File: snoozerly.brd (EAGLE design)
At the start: 70 x 43 mm, 57 parts, among them Q2 MOSFET-NCHANNELFDD8780, Q3 MOSFET-NCHANNELBSS123LT1G, Q4 MOSFET-NCHANNELBSS123LT1G, U1 ATMEGA328P, Y1 32KHz, Y2 8MHz

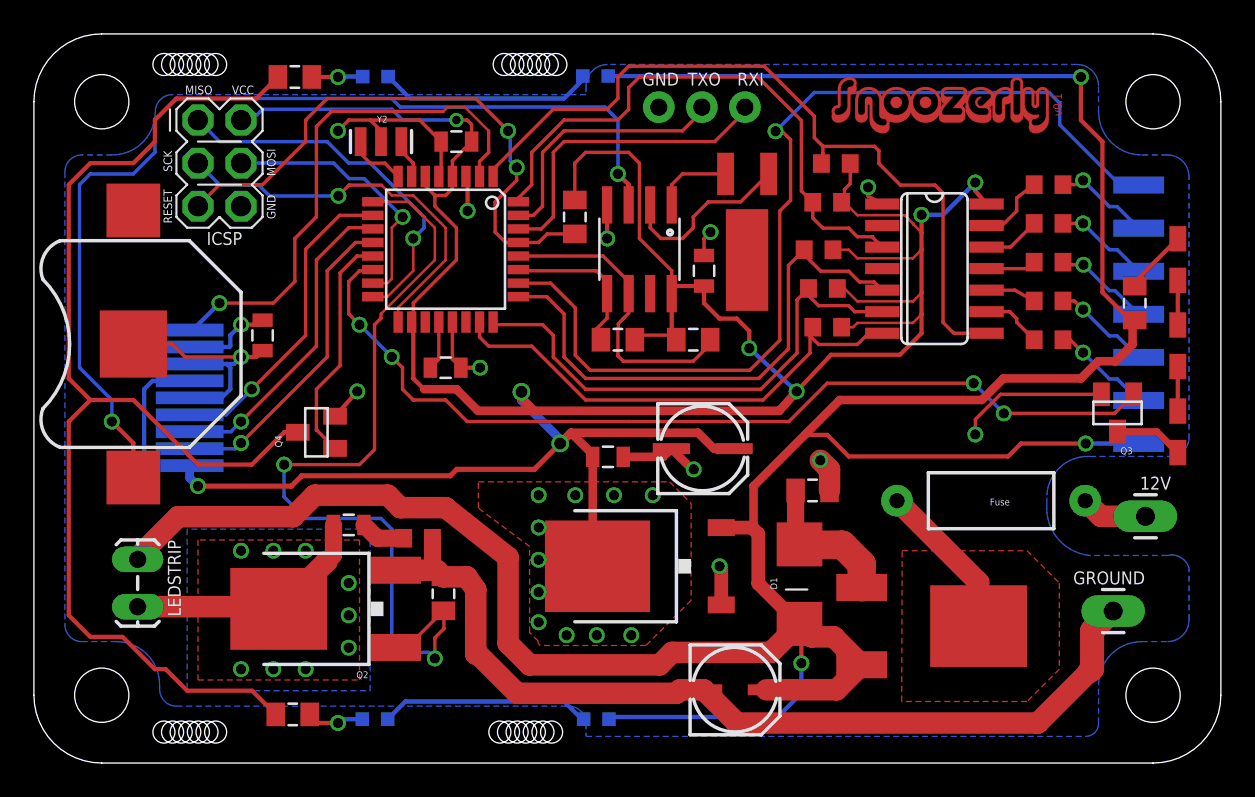
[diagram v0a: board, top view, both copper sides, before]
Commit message: update pchannel footprint and fixed spacings
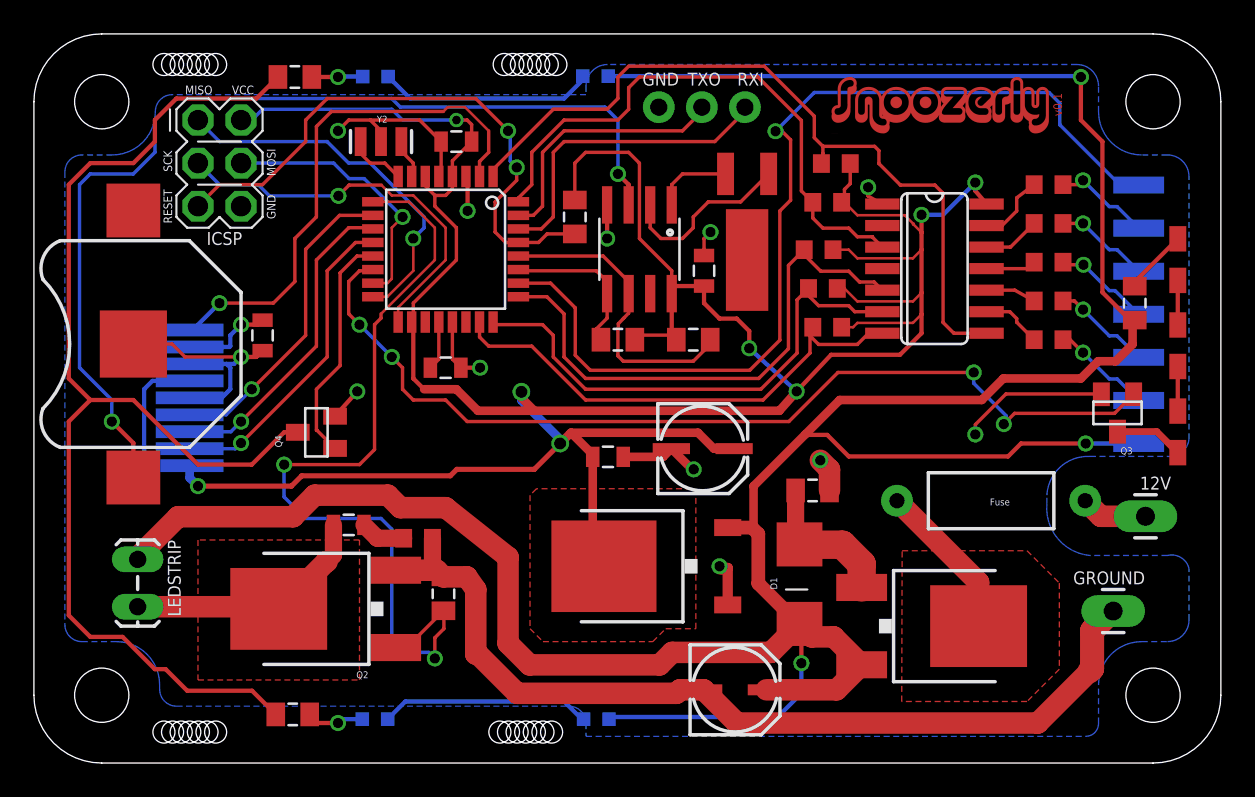
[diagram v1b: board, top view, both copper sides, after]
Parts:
- removed U$26: VREG-3.3VNCP1117, jt_parts:TO-252
- added NCP1117: VREG-3.3VNCP1117, jt_parts:TO-252
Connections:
- net 12V: now also NCP1117.3; no longer U$26.3
- net 5V: now also NCP1117.2; no longer U$26.2
- net GND: now also NCP1117.1; no longer U$26.1
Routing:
- net NIGHT_LIGHT: track 55.4 -> 57.3 mm
- net N$14: vias 9 -> 0
- removed copper zone on layer 16, net N$14
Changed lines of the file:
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@@
 <attribute name="VALUE" x="23.876" y="14.859" size="0.4064" layer="27" rot="R180"/>
 </element>
-<element name="U$26" library="jt_parts" package="TO-252" value="VREG-3.3VNCP1117" x="34.925" y="12.065" rot="R90"/>
+<element name="NCP1117" library="jt_parts" package="TO-252" value="VREG-3.3VNCP1117" x="35.306" y="12.065" rot="R90"/>
 </elements>
 <signals>
@@
 <contactref element="GROUND" pad="1"/>
 <wire x1="62.7126" y1="5.8674" x2="59.6646" y2="2.8194" width="1.27" layer="1"/>
-<wire x1="63.4136" y1="22.2074" x2="57.4626" y2="22.2074" width="0.2032" layer="1"/>
-<wire x1="57.4626" y1="22.2074" x2="55.9816" y2="20.7264" width="0.2032" layer="1"/>
 <via x="55.9816" y="19.8374" extent="1-16" drill="0.6"/>
-<wire x1="55.9816" y1="20.7264" x2="55.9816" y2="19.8374" width="0.2032" layer="1"/>
 <via x="26.035" y="33.02" extent="1-16" drill="0.6"/>
 <wire x1="26.035" y1="33.02" x2="26.035" y2="34.9566" width="0.254" layer="1"/>
@@
 <wire x1="47.3804" y1="17.7706" x2="46.8376" y2="18.3134" width="1.27" layer="1"/>
 <contactref element="SERIAL" pad="1"/>
-<contactref element="U$26" pad="1"/>
+<contactref element="NCP1117" pad="1"/>
 <via x="40.894" y="12.065" extent="1-16" drill="0.6"/>
-<wire x1="40.995" y1="9.785" x2="40.995" y2="11.964" width="0.8128" layer="1"/>
 <wire x1="40.995" y1="11.964" x2="40.894" y2="12.065" width="0.8128" layer="1"/>
 <wire x1="35.2154" y1="18.5166" x2="37.5668" y2="18.5166" width="0.508" layer="1"/>
 <wire x1="37.5668" y1="18.5166" x2="38.0526" y2="19.0024" width="0.508" layer="1"/>
 <via x="39.37" y="17.78" extent="1-16" drill="0.6"/>
-<wire x1="64.1096" y1="9.4996" x2="64.1096" y2="9.4234" width="0" layer="19" extent="1-1"/>
 <wire x1="39.37" y1="17.78" x2="39.275" y2="17.78" width="0.508" layer="1"/>
 <wire x1="39.275" y1="17.78" x2="38.0526" y2="19.0024" width="0.508" layer="1"/>
+<wire x1="40.995" y1="11.964" x2="41.376" y2="11.964" width="0.6096" layer="1"/>
+<wire x1="41.376" y1="11.964" x2="41.376" y2="9.785" width="0.6096" layer="1"/>
+<wire x1="55.9816" y1="19.8374" x2="55.9816" y2="20.4216" width="0.2032" layer="1"/>
+<wire x1="55.9816" y1="20.4216" x2="57.785" y2="22.225" width="0.2032" layer="1"/>
+<wire x1="57.785" y1="22.225" x2="63.396" y2="22.225" width="0.2032" layer="1"/>
+<wire x1="63.396" y1="22.225" x2="63.4136" y2="22.2074" width="0.2032" layer="1"/>
+<wire x1="64.1096" y1="9.4234" x2="64.1096" y2="9.4996" width="0" layer="19" extent="1-1"/>
 </signal>
 <signal name="5V" class="2">
@@
 <wire x1="25.4" y1="17.78" x2="29.972" y2="17.78" width="0.3048" layer="1"/>
 <wire x1="29.972" y1="17.78" x2="31.496" y2="19.304" width="0.3048" layer="1"/>
-<contactref element="U$26" pad="2"/>
-<polygon width="0" layer="1" thermals="no">
-<vertex x="29.6926" y="8.1534"/>
-<vertex x="29.6926" y="13.2334"/>
-<vertex x="26.67" y="15.494"/>
-<vertex x="26.67" y="17.0434"/>
-<vertex x="37.9476" y="17.0434"/>
-<vertex x="39.2176" y="15.7734"/>
-<vertex x="39.2176" y="10.0584"/>
-<vertex x="36.5506" y="7.3914"/>
-<vertex x="30.3276" y="7.3914"/>
-<vertex x="30.2006" y="7.5184"/>
-<vertex x="30.2006" y="7.6454"/>
-</polygon>
+<contactref element="NCP1117" pad="2"/>
 <wire x1="41.3226" y1="19.0024" x2="40.5606" y2="19.0024" width="0.508" layer="1"/>
 <wire x1="40.5606" y1="19.0024" x2="39.624" y2="19.939" width="0.508" layer="1"/>
@@
 <wire x1="33.4154" y1="18.6546" x2="32.131" y2="19.939" width="0.508" layer="1"/>
 <wire x1="33.4154" y1="18.5166" x2="33.4154" y2="12.3446" width="0.508" layer="1"/>
-<wire x1="33.4154" y1="12.3446" x2="33.695" y2="12.065" width="0.508" layer="1"/>
+<wire x1="33.4154" y1="12.3446" x2="34.076" y2="12.065" width="0.508" layer="1"/>
+<polygon width="0.0254" layer="1" thermals="no">
+<vertex x="29.718" y="16.256"/>
+<vertex x="29.718" y="8.382"/>
+<vertex x="30.48" y="7.62"/>
+<vertex x="36.957" y="7.62"/>
+<vertex x="37.719" y="8.382"/>
+<vertex x="39.497" y="8.382"/>
+<vertex x="39.497" y="16.383"/>
+<vertex x="39.243" y="16.637"/>
+<vertex x="30.099" y="16.637"/>
+</polygon>
 </signal>
 <signal name="N$64">
@@
 <wire x1="17.018" y1="16.256" x2="15.748" y2="14.986" width="1.27" layer="1"/>
 <wire x1="15.748" y1="14.986" x2="8.9662" y2="14.986" width="1.27" layer="1"/>
-<contactref element="U$26" pad="3"/>
+<contactref element="NCP1117" pad="3"/>
 <wire x1="37.3634" y1="6.2484" x2="38.1" y2="6.985" width="1.27" layer="1"/>
 <wire x1="38.1" y1="6.985" x2="43.9322" y2="6.985" width="1.27" layer="1"/>
 <wire x1="43.9322" y1="6.985" x2="45.6106" y2="8.6634" width="1.27" layer="1"/>
-<wire x1="40.995" y1="14.345" x2="42.805" y2="14.345" width="0.8128" layer="1"/>
+<wire x1="41.376" y1="14.345" x2="42.805" y2="14.345" width="0.8128" layer="1"/>
 <wire x1="42.805" y1="14.345" x2="43.18" y2="13.97" width="0.8128" layer="1"/>
 <wire x1="43.18" y1="13.97" x2="43.18" y2="11.049" width="0.8128" layer="1"/>
@@
 <vertex x="19.6596" y="5.3594"/>
 </polygon>
-<via x="16.4846" y="5.9944" extent="1-16" drill="0.6"/>
-<via x="14.5796" y="5.9944" extent="1-16" drill="0.6"/>
-<via x="12.6746" y="5.9944" extent="1-16" drill="0.6"/>
-<via x="16.4846" y="12.9794" extent="1-16" drill="0.6"/>
-<via x="14.5796" y="12.9794" extent="1-16" drill="0.6"/>
-<via x="12.6746" y="12.9794" extent="1-16" drill="0.6"/>
-<via x="19.0246" y="7.2644" extent="1-16" drill="0.6"/>
-<via x="19.0246" y="11.0744" extent="1-16" drill="0.6"/>
-<polygon width="0" layer="16" thermals="no">
-<vertex x="20.2946" y="4.7244"/>
-<vertex x="20.2946" y="14.2494"/>
-<vertex x="9.4996" y="14.2494"/>
-<vertex x="9.4996" y="4.7244"/>
-</polygon>
 <wire x1="17.7546" y1="12.3444" x2="17.7146" y2="12.3444" width="1.27" layer="1"/>
 <wire x1="17.7146" y1="12.3444" x2="15.2146" y2="9.8444" width="1.27" layer="1"/>
@@
 <wire x1="15.2146" y1="9.8044" x2="15.1506" y2="9.8044" width="1.27" layer="1"/>
 <wire x1="15.1506" y1="9.8044" x2="14.8966" y2="9.5504" width="1.27" layer="1"/>
-<via x="19.0246" y="9.1694" extent="1-16" drill="0.6"/>
 <wire x1="6.5786" y1="9.6774" x2="15.7226" y2="9.6774" width="1.27" layer="1"/>
 <wire x1="15.7226" y1="9.6774" x2="16.51" y2="8.89" width="1.27" layer="1"/>
@@
 <wire x1="26.0096" y1="20.5994" x2="24.7396" y2="21.8694" width="0.2032" layer="1"/>
 <wire x1="24.7396" y1="21.8694" x2="22.8346" y2="21.8694" width="0.2032" layer="1"/>
-<wire x1="35.5346" y1="20.5994" x2="26.0096" y2="20.5994" width="0.2032" layer="1"/>
+<wire x1="44.9834" y1="20.5994" x2="26.0096" y2="20.5994" width="0.2032" layer="1"/>
 <wire x1="22.8346" y1="21.8694" x2="22.1996" y2="22.5044" width="0.2032" layer="1"/>
 <wire x1="22.1996" y1="22.5044" x2="22.1996" y2="23.7744" width="0.2032" layer="1"/>
@@
 <wire x1="19.6596" y1="29.4894" x2="20.377" y2="29.4894" width="0.2032" layer="1"/>
 <wire x1="20.377" y1="29.4894" x2="20.447" y2="29.5594" width="0.2032" layer="1"/>
-<wire x1="35.5346" y1="20.5994" x2="44.9834" y2="20.5994" width="0.2032" layer="1"/>
-<wire x1="44.9834" y1="20.5994" x2="47.244" y2="22.86" width="0.2032" layer="1"/>
-<wire x1="47.244" y1="22.86" x2="55.88" y2="22.86" width="0.2032" layer="1"/>
-<via x="55.88" y="22.86" extent="1-16" drill="0.6"/>
-<via x="57.658" y="21.082" extent="1-16" drill="0.6"/>
-<wire x1="57.658" y1="21.082" x2="64.1882" y2="21.082" width="0.2032" layer="1"/>
+<wire x1="44.9834" y1="20.5994" x2="47.879" y2="23.495" width="0.2032" layer="1"/>
+<via x="55.88" y="23.495" extent="1-16" drill="0.6"/>
+<via x="57.658" y="20.447" extent="1-16" drill="0.6"/>
 <wire x1="64.1882" y1="21.082" x2="65.3136" y2="22.2074" width="0.2032" layer="1"/>
-<wire x1="57.658" y1="21.082" x2="55.88" y2="22.86" width="0.2032" layer="16"/>
+<wire x1="55.88" y1="23.495" x2="47.879" y2="23.495" width="0.2032" layer="1"/>
+<wire x1="64.1882" y1="21.082" x2="58.293" y2="21.082" width="0.2032" layer="1"/>
+<wire x1="58.293" y1="21.082" x2="57.658" y2="20.447" width="0.2032" layer="1"/>
+<wire x1="55.88" y1="23.495" x2="55.88" y2="22.86" width="0.2032" layer="16"/>
+<wire x1="55.88" y1="22.86" x2="57.785" y2="20.955" width="0.2032" layer="16"/>
+<wire x1="57.785" y1="20.955" x2="57.785" y2="20.574" width="0.2032" layer="16"/>
+<wire x1="57.785" y1="20.574" x2="57.658" y2="20.447" width="0.2032" layer="16"/>
 </signal>
 <signal name="N$19">
@@
 <wire x1="20.712" y1="13.716" x2="19.9246" y2="14.5034" width="1.016" layer="1"/>
 </signal>
-<signal name="N$24">
-<via x="34.671" y="16.256" extent="1-16" drill="0.6"/>
-</signal>
-<signal name="N$25">
-<via x="32.385" y="16.256" extent="1-16" drill="0.6"/>
-</signal>
-<signal name="N$26">
-<via x="36.957" y="16.256" extent="1-16" drill="0.6"/>
-</signal>
-<signal name="N$27">
-<via x="30.226" y="16.256" extent="1-16" drill="0.6"/>
-</signal>
-<signal name="N$29">
-<via x="30.226" y="14.351" extent="1-16" drill="0.6"/>
-</signal>
-<signal name="N$34">
-<via x="30.226" y="12.446" extent="1-16" drill="0.6"/>
-</signal>
-<signal name="N$35">
-<via x="30.226" y="10.541" extent="1-16" drill="0.6"/>
-</signal>
-<signal name="N$36">
-<via x="30.226" y="8.763" extent="1-16" drill="0.6"/>
-</signal>
-<signal name="N$37">
-<via x="31.877" y="8.001" extent="1-16" drill="0.6"/>
-</signal>
-<signal name="N$38">
-<via x="33.655" y="8.001" extent="1-16" drill="0.6"/>
-</signal>
-<signal name="N$39">
-<via x="35.687" y="8.001" extent="1-16" drill="0.6"/>
-</signal>
 </signals>

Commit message: Merge branch 'master' into rev-0.1
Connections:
- net PWM_LED renamed PWM_STRIP
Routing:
- net PWM_STRIP: track 49.9 -> 47.8 mm
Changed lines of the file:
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@@
 <wire x1="24.8666" y1="39.1414" x2="25.8826" y2="39.1414" width="0.1524" layer="1"/>
-</signal>
-<signal name="PWM_LED">
-<contactref element="U1" pad="9"/>
-<contactref element="U$15" pad="2"/>
-<contactref element="Q2" pad="1"/>
-<wire x1="20.447" y1="33.5594" x2="22.5746" y2="33.5594" width="0.1524" layer="1"/>
-<wire x1="22.5746" y1="33.5594" x2="24.1046" y2="32.0294" width="0.1524" layer="1"/>
-<via x="24.1046" y="6.6294" extent="1-16" drill="0.6"/>
-<via x="15.2146" y="18.0594" extent="1-16" drill="0.6"/>
-<wire x1="24.1046" y1="32.0294" x2="24.1046" y2="30.1244" width="0.1524" layer="1"/>
-<wire x1="20.5486" y1="26.3144" x2="20.5486" y2="18.9484" width="0.2032" layer="1"/>
-<wire x1="20.5486" y1="18.9484" x2="19.6596" y2="18.0594" width="0.2032" layer="1"/>
-<wire x1="19.6596" y1="18.0594" x2="15.2146" y2="18.0594" width="0.2032" layer="1"/>
-<wire x1="15.2146" y1="18.0594" x2="15.2146" y2="16.1544" width="0.2032" layer="16"/>
-<wire x1="15.2146" y1="16.1544" x2="16.4846" y2="14.8844" width="0.2032" layer="16"/>
-<wire x1="16.4846" y1="14.8844" x2="20.9296" y2="14.8844" width="0.2032" layer="16"/>
-<wire x1="20.9296" y1="14.8844" x2="21.5646" y2="14.2494" width="0.2032" layer="16"/>
-<wire x1="24.1046" y1="30.1244" x2="20.9296" y2="26.9494" width="0.1524" layer="1"/>
-<wire x1="20.9296" y1="26.9494" x2="20.9296" y2="26.6954" width="0.2032" layer="1"/>
-<wire x1="20.9296" y1="26.6954" x2="20.5486" y2="26.3144" width="0.2032" layer="1"/>
-<wire x1="24.1046" y1="7.8486" x2="24.638" y2="8.382" width="0.2032" layer="1"/>
-<wire x1="24.638" y1="8.382" x2="24.638" y2="9.414" width="0.2032" layer="1"/>
-<wire x1="24.638" y1="9.414" x2="24.6126" y2="9.4394" width="0.2032" layer="1"/>
-<wire x1="21.5646" y1="14.2494" x2="21.5646" y2="7.6454" width="0.2032" layer="16"/>
-<wire x1="21.5646" y1="7.6454" x2="22.225" y2="6.985" width="0.2032" layer="16"/>
-<wire x1="22.225" y1="6.985" x2="23.749" y2="6.985" width="0.2032" layer="16"/>
-<wire x1="23.749" y1="6.985" x2="24.1046" y2="6.6294" width="0.2032" layer="16"/>
-<wire x1="24.1046" y1="7.8486" x2="24.1046" y2="6.6294" width="0.2032" layer="1"/>
-<wire x1="21.7946" y1="7.2704" x2="22.4436" y2="7.2704" width="0.2032" layer="1"/>
-<wire x1="22.4436" y1="7.2704" x2="24.6126" y2="9.4394" width="0.2032" layer="1"/>
 </signal>
 <signal name="12V">
@@
 <wire x1="20.712" y1="13.716" x2="19.9246" y2="14.5034" width="1.016" layer="1"/>
 </signal>
+<signal name="PWM_STRIP">
+<contactref element="U1" pad="9"/>
+<contactref element="U$15" pad="2"/>
+<contactref element="Q2" pad="1"/>
+<wire x1="22.5746" y1="33.5594" x2="24.1046" y2="32.0294" width="0.1524" layer="1"/>
+<via x="24.1046" y="6.6294" extent="1-16" drill="0.6"/>
+<via x="15.2146" y="18.0594" extent="1-16" drill="0.6"/>
+<wire x1="24.1046" y1="32.0294" x2="24.1046" y2="30.1244" width="0.1524" layer="1"/>
+<wire x1="20.5486" y1="26.3144" x2="20.5486" y2="18.9484" width="0.2032" layer="1"/>
+<wire x1="20.5486" y1="18.9484" x2="19.6596" y2="18.0594" width="0.2032" layer="1"/>
+<wire x1="19.6596" y1="18.0594" x2="15.2146" y2="18.0594" width="0.2032" layer="1"/>
+<wire x1="15.2146" y1="18.0594" x2="15.2146" y2="16.1544" width="0.2032" layer="16"/>
+<wire x1="15.2146" y1="16.1544" x2="16.4846" y2="14.8844" width="0.2032" layer="16"/>
+<wire x1="16.4846" y1="14.8844" x2="20.9296" y2="14.8844" width="0.2032" layer="16"/>
+<wire x1="20.9296" y1="14.8844" x2="21.5646" y2="14.2494" width="0.2032" layer="16"/>
+<wire x1="24.1046" y1="30.1244" x2="20.9296" y2="26.9494" width="0.1524" layer="1"/>
+<wire x1="20.9296" y1="26.9494" x2="20.9296" y2="26.6954" width="0.2032" layer="1"/>
+<wire x1="20.9296" y1="26.6954" x2="20.5486" y2="26.3144" width="0.2032" layer="1"/>
+<wire x1="24.1046" y1="7.8486" x2="24.638" y2="8.382" width="0.2032" layer="1"/>
+<wire x1="24.638" y1="8.382" x2="24.638" y2="9.414" width="0.2032" layer="1"/>
+<wire x1="24.638" y1="9.414" x2="24.6126" y2="9.4394" width="0.2032" layer="1"/>
+<wire x1="21.5646" y1="14.2494" x2="21.5646" y2="7.6454" width="0.2032" layer="16"/>
+<wire x1="21.5646" y1="7.6454" x2="22.225" y2="6.985" width="0.2032" layer="16"/>
+<wire x1="22.225" y1="6.985" x2="23.749" y2="6.985" width="0.2032" layer="16"/>
+<wire x1="23.749" y1="6.985" x2="24.1046" y2="6.6294" width="0.2032" layer="16"/>
+<wire x1="24.1046" y1="7.8486" x2="24.1046" y2="6.6294" width="0.2032" layer="1"/>
+<wire x1="21.7946" y1="7.2704" x2="22.4436" y2="7.2704" width="0.2032" layer="1"/>
+<wire x1="22.4436" y1="7.2704" x2="24.6126" y2="9.4394" width="0.2032" layer="1"/>
+<wire x1="22.5746" y1="33.5594" x2="20.447" y2="33.5594" width="0" layer="19" extent="1-1"/>
+</signal>
 </signals>
